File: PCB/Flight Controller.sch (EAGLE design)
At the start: 10 parts, among them J1 ZX62-AB-5PA(31), J2 M50-3600542R, U1 BMP390L, U2 NINA-B306, U3 LMS8117ADT-3.3, U4 BNO055

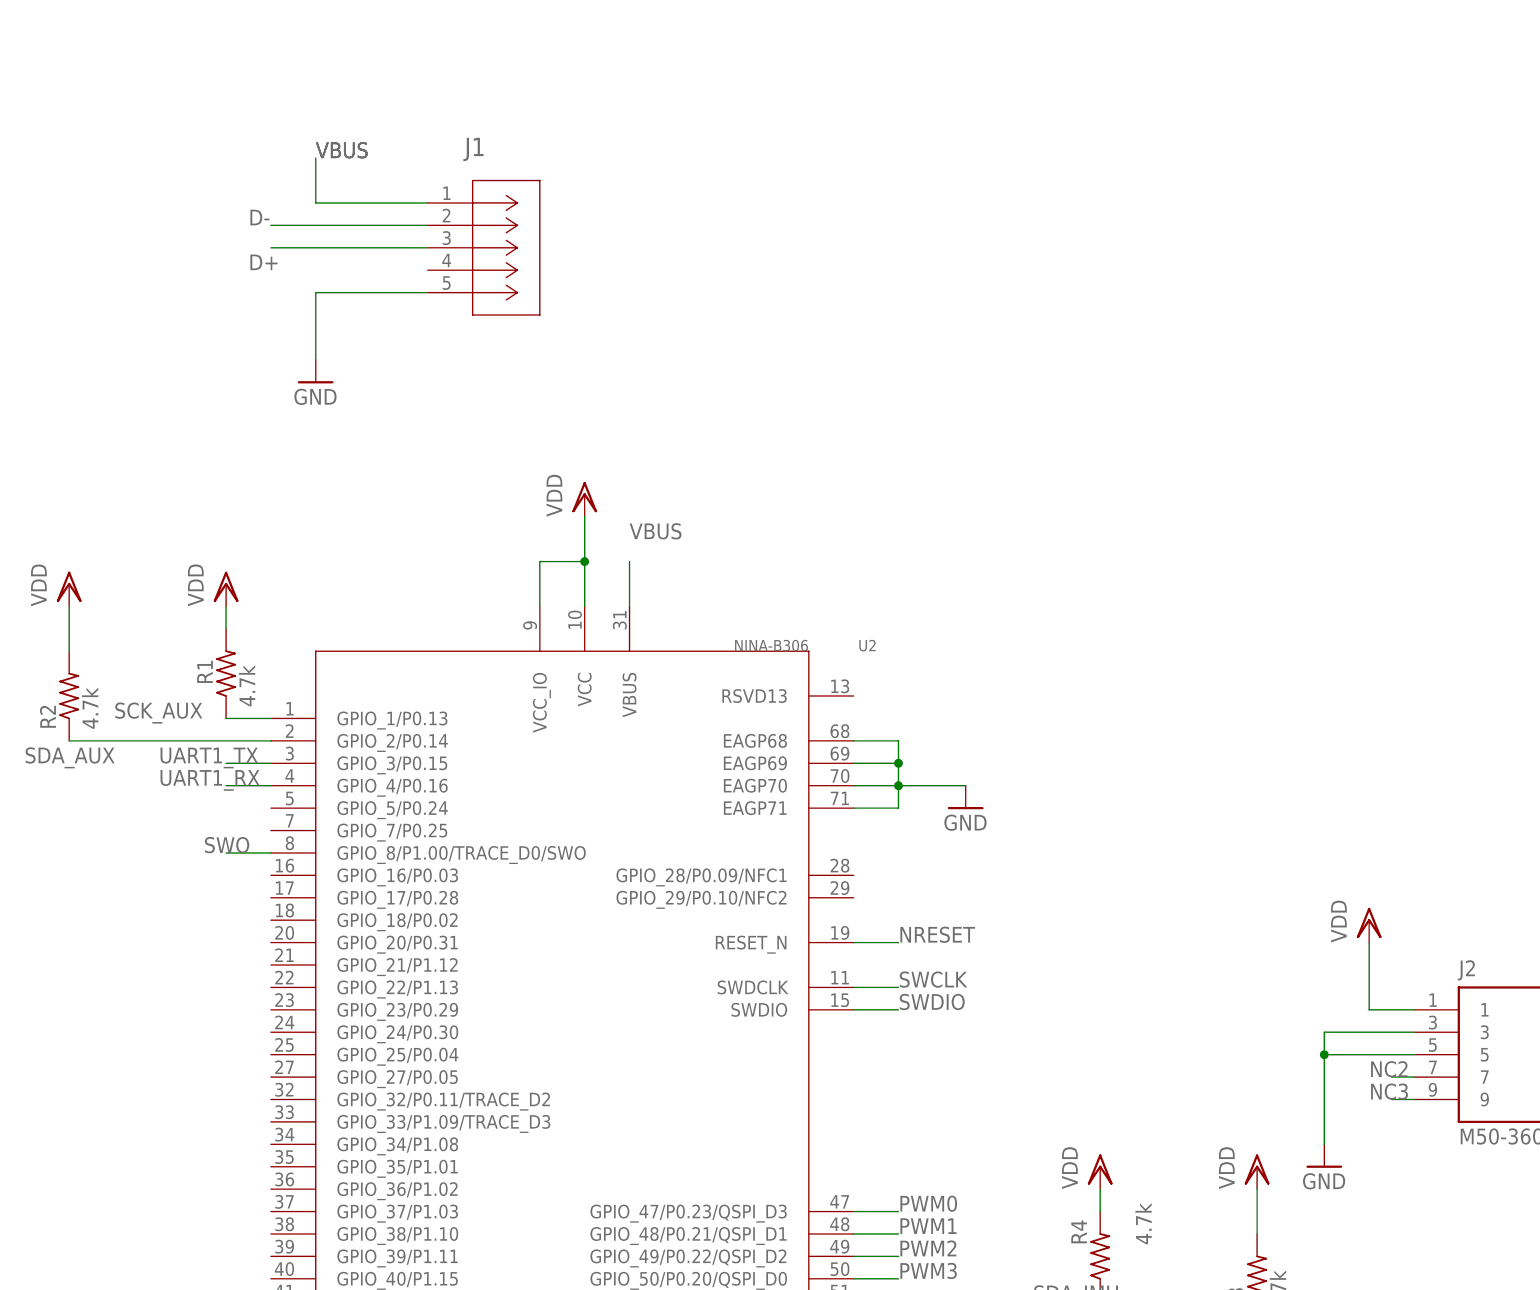
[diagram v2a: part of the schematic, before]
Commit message: added LEDs to PCB
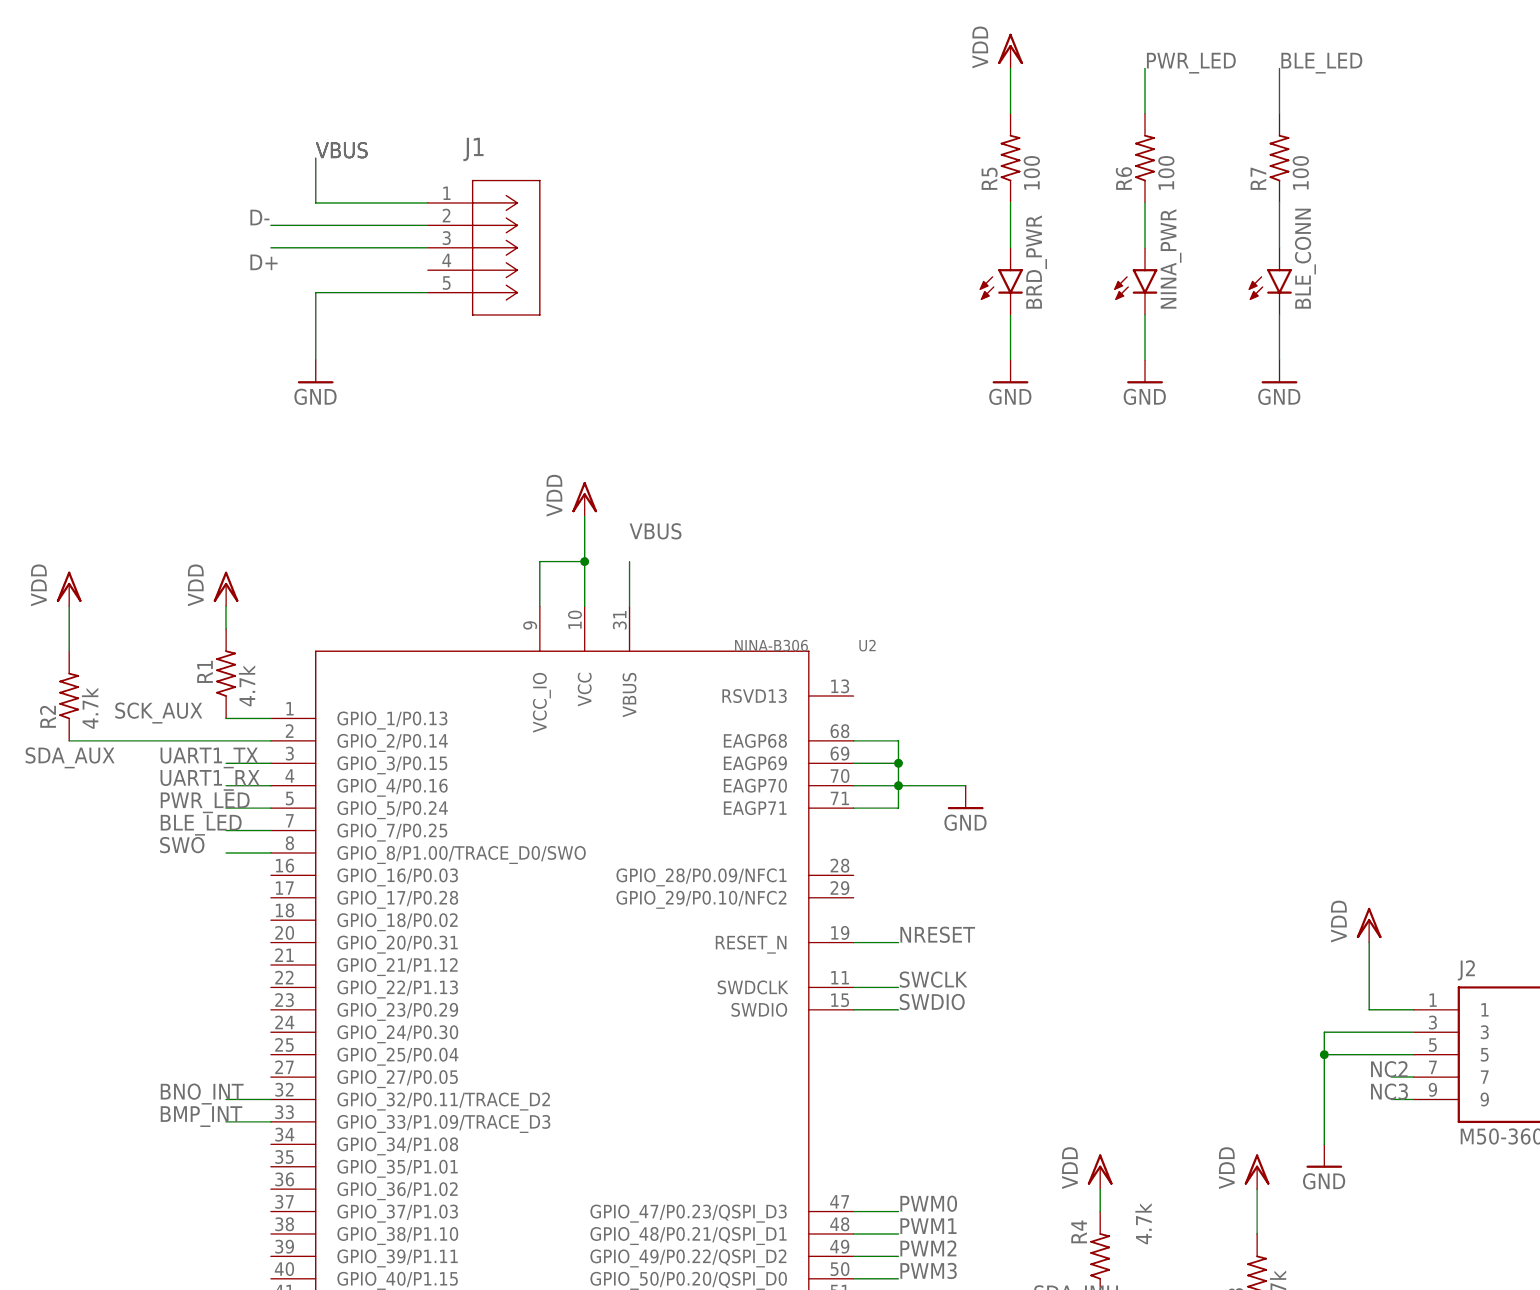
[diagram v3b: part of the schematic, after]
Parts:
- added BLE_CONN, BRD_PWR, NINA_PWR: (no value), led:LEDCHIPLED_1206
- added R5, R6, R7: 100, rcl:R-US_R1206
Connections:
- new net BLE_LED: R7.2, U2.GPIO_7/P0.25
- new net N$1: BRD_PWR.A, R5.1
- new net N$2: NINA_PWR.A, R6.1
- new net N$3: BLE_CONN.A, R7.1
- new net PWR_LED: R6.2, U2.GPIO_5/P0.24
- net BMP_INT: now also U2.GPIO_33/P1.09/TRACE_D3
- net BNO_INT: now also U2.GPIO_32/P0.11/TRACE_D2
- net GND: now also BLE_CONN.C, BRD_PWR.C, NINA_PWR.C
- net VDD: now also R5.2
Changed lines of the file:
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@@
 <part name="VDD10" library="supply1" library_urn="urn:adsk.eagle:library:371" deviceset="VDD" device=""/>
 <part name="VDD11" library="supply1" library_urn="urn:adsk.eagle:library:371" deviceset="VDD" device=""/>
+<part name="BRD_PWR" library="led" library_urn="urn:adsk.eagle:library:259" deviceset="LED" device="CHIPLED_1206" package3d_urn="urn:adsk.eagle:package:15823/2"/>
+<part name="NINA_PWR" library="led" library_urn="urn:adsk.eagle:library:259" deviceset="LED" device="CHIPLED_1206" package3d_urn="urn:adsk.eagle:package:15823/2"/>
+<part name="BLE_CONN" library="led" library_urn="urn:adsk.eagle:library:259" deviceset="LED" device="CHIPLED_1206" package3d_urn="urn:adsk.eagle:package:15823/2"/>
+<part name="R5" library="rcl" library_urn="urn:adsk.eagle:library:334" deviceset="R-US_" device="R1206" package3d_urn="urn:adsk.eagle:package:23540/2" value="100"/>
+<part name="R6" library="rcl" library_urn="urn:adsk.eagle:library:334" deviceset="R-US_" device="R1206" package3d_urn="urn:adsk.eagle:package:23540/2" value="100"/>
+<part name="R7" library="rcl" library_urn="urn:adsk.eagle:library:334" deviceset="R-US_" device="R1206" package3d_urn="urn:adsk.eagle:package:23540/2" value="100"/>
+<part name="GND10" library="supply1" library_urn="urn:adsk.eagle:library:371" deviceset="GND" device=""/>
+<part name="GND11" library="supply1" library_urn="urn:adsk.eagle:library:371" deviceset="GND" device=""/>
+<part name="GND12" library="supply1" library_urn="urn:adsk.eagle:library:371" deviceset="GND" device=""/>
+<part name="VDD12" library="supply1" library_urn="urn:adsk.eagle:library:371" deviceset="VDD" device=""/>
 </parts>
 <sheets>
@@
 <attribute name="VALUE" x="284.48" y="58.42" size="1.778" layer="96" rot="R90"/>
 </instance>
+<instance part="BRD_PWR" gate="G$1" x="259.08" y="162.56" smashed="yes">
+<attribute name="NAME" x="262.636" y="157.988" size="1.778" layer="95" rot="R90"/>
+<attribute name="VALUE" x="264.795" y="157.988" size="1.778" layer="96" rot="R90"/>
+</instance>
+<instance part="NINA_PWR" gate="G$1" x="274.32" y="162.56" smashed="yes">
+<attribute name="NAME" x="277.876" y="157.988" size="1.778" layer="95" rot="R90"/>
+<attribute name="VALUE" x="280.035" y="157.988" size="1.778" layer="96" rot="R90"/>
+</instance>
+<instance part="BLE_CONN" gate="G$1" x="289.56" y="162.56" smashed="yes">
+<attribute name="NAME" x="293.116" y="157.988" size="1.778" layer="95" rot="R90"/>
+<attribute name="VALUE" x="295.275" y="157.988" size="1.778" layer="96" rot="R90"/>
+</instance>
+<instance part="R5" gate="G$1" x="259.08" y="175.26" smashed="yes" rot="R90">
+<attribute name="NAME" x="257.5814" y="171.45" size="1.778" layer="95" rot="R90"/>
+<attribute name="VALUE" x="262.382" y="171.45" size="1.778" layer="96" rot="R90"/>
+</instance>
+<instance part="R6" gate="G$1" x="274.32" y="175.26" smashed="yes" rot="R90">
+<attribute name="NAME" x="272.8214" y="171.45" size="1.778" layer="95" rot="R90"/>
+<attribute name="VALUE" x="277.622" y="171.45" size="1.778" layer="96" rot="R90"/>
+</instance>
+<instance part="R7" gate="G$1" x="289.56" y="175.26" smashed="yes" rot="R90">
+<attribute name="NAME" x="288.0614" y="171.45" size="1.778" layer="95" rot="R90"/>
+<attribute name="VALUE" x="292.862" y="171.45" size="1.778" layer="96" rot="R90"/>
+</instance>
+<instance part="GND10" gate="1" x="259.08" y="149.86" smashed="yes">
+<attribute name="VALUE" x="256.54" y="147.32" size="1.778" layer="96"/>
+</instance>
+<instance part="GND11" gate="1" x="274.32" y="149.86" smashed="yes">
+<attribute name="VALUE" x="271.78" y="147.32" size="1.778" layer="96"/>
+</instance>
+<instance part="GND12" gate="1" x="289.56" y="149.86" smashed="yes">
+<attribute name="VALUE" x="287.02" y="147.32" size="1.778" layer="96"/>
+</instance>
+<instance part="VDD12" gate="G$1" x="259.08" y="187.96" smashed="yes">
+<attribute name="VALUE" x="256.54" y="185.42" size="1.778" layer="96" rot="R90"/>
+</instance>
 </instances>
 <busses>
@@
 <wire x1="287.02" y1="53.34" x2="287.02" y2="58.42" width="0.1524" layer="91"/>
 <pinref part="VDD11" gate="G$1" pin="VDD"/>
+</segment>
+<segment>
+<pinref part="R5" gate="G$1" pin="2"/>
+<pinref part="VDD12" gate="G$1" pin="VDD"/>
+<wire x1="259.08" y1="185.42" x2="259.08" y2="180.34" width="0.1524" layer="91"/>
 </segment>
 </net>
@@
 <junction x="71.12" y="55.88"/>
 </segment>
+<segment>
+<pinref part="BRD_PWR" gate="G$1" pin="C"/>
+<wire x1="259.08" y1="157.48" x2="259.08" y2="152.4" width="0.1524" layer="91"/>
+<pinref part="GND10" gate="1" pin="GND"/>
+</segment>
+<segment>
+<pinref part="NINA_PWR" gate="G$1" pin="C"/>
+<wire x1="274.32" y1="157.48" x2="274.32" y2="152.4" width="0.1524" layer="91"/>
+<pinref part="GND11" gate="1" pin="GND"/>
+</segment>
+<segment>
+<pinref part="BLE_CONN" gate="G$1" pin="C"/>
+<wire x1="289.56" y1="157.48" x2="289.56" y2="152.4" width="0.1524" layer="91"/>
+<pinref part="GND12" gate="1" pin="GND"/>
+</segment>
 </net>
 <net name="D-" class="0">
@@
 <pinref part="U2" gate="A" pin="GPIO_8/P1.00/TRACE_D0/SWO"/>
 <wire x1="175.26" y1="96.52" x2="170.18" y2="96.52" width="0.1524" layer="91"/>
-<label x="167.64" y="96.52" size="1.778" layer="95"/>
+<label x="162.56" y="96.52" size="1.778" layer="95"/>
 </segment>
 </net>
@@
 <wire x1="121.92" y1="68.58" x2="127" y2="68.58" width="0.1524" layer="91"/>
 <label x="127" y="68.58" size="1.778" layer="95"/>
+</segment>
+<segment>
+<pinref part="U2" gate="A" pin="GPIO_32/P0.11/TRACE_D2"/>
+<wire x1="175.26" y1="68.58" x2="170.18" y2="68.58" width="0.1524" layer="91"/>
+<label x="162.56" y="68.58" size="1.778" layer="95"/>
 </segment>
 </net>
@@
 <label x="129.54" y="147.32" size="1.778" layer="95"/>
 </segment>
+<segment>
+<pinref part="U2" gate="A" pin="GPIO_33/P1.09/TRACE_D3"/>
+<wire x1="175.26" y1="66.04" x2="170.18" y2="66.04" width="0.1524" layer="91"/>
+<label x="162.56" y="66.04" size="1.778" layer="95"/>
+</segment>
 </net>
 <net name="NC3" class="0">
@@
 </segment>
 </net>
+<net name="N$1" class="0">
+<segment>
+<pinref part="R5" gate="G$1" pin="1"/>
+<pinref part="BRD_PWR" gate="G$1" pin="A"/>
+<wire x1="259.08" y1="170.18" x2="259.08" y2="165.1" width="0.1524" layer="91"/>
+</segment>
+</net>
+<net name="N$2" class="0">
+<segment>
+<pinref part="R6" gate="G$1" pin="1"/>
+<pinref part="NINA_PWR" gate="G$1" pin="A"/>
+<wire x1="274.32" y1="170.18" x2="274.32" y2="165.1" width="0.1524" layer="91"/>
+</segment>
+</net>
+<net name="N$3" class="0">
+<segment>
+<pinref part="R7" gate="G$1" pin="1"/>
+<pinref part="BLE_CONN" gate="G$1" pin="A"/>
+<wire x1="289.56" y1="170.18" x2="289.56" y2="165.1" width="0.1524" layer="91"/>
+</segment>
+</net>
+<net name="PWR_LED" class="0">
+<segment>
+<pinref part="R6" gate="G$1" pin="2"/>
+<wire x1="274.32" y1="180.34" x2="274.32" y2="185.42" width="0.1524" layer="91"/>
+<label x="274.32" y="185.42" size="1.778" layer="95"/>
+</segment>
+<segment>
+<pinref part="U2" gate="A" pin="GPIO_5/P0.24"/>
+<wire x1="175.26" y1="101.6" x2="170.18" y2="101.6" width="0.1524" layer="91"/>
+<label x="162.56" y="101.6" size="1.778" layer="95"/>
+</segment>
+</net>
+<net name="BLE_LED" class="0">
+<segment>
+<pinref part="R7" gate="G$1" pin="2"/>
+<wire x1="289.56" y1="180.34" x2="289.56" y2="185.42" width="0.1524" layer="91"/>
+<label x="289.56" y="185.42" size="1.778" layer="95"/>
+</segment>
+<segment>
+<pinref part="U2" gate="A" pin="GPIO_7/P0.25"/>
+<wire x1="175.26" y1="99.06" x2="170.18" y2="99.06" width="0.1524" layer="91"/>
+<label x="162.56" y="99.06" size="1.778" layer="95"/>
+</segment>
+</net>

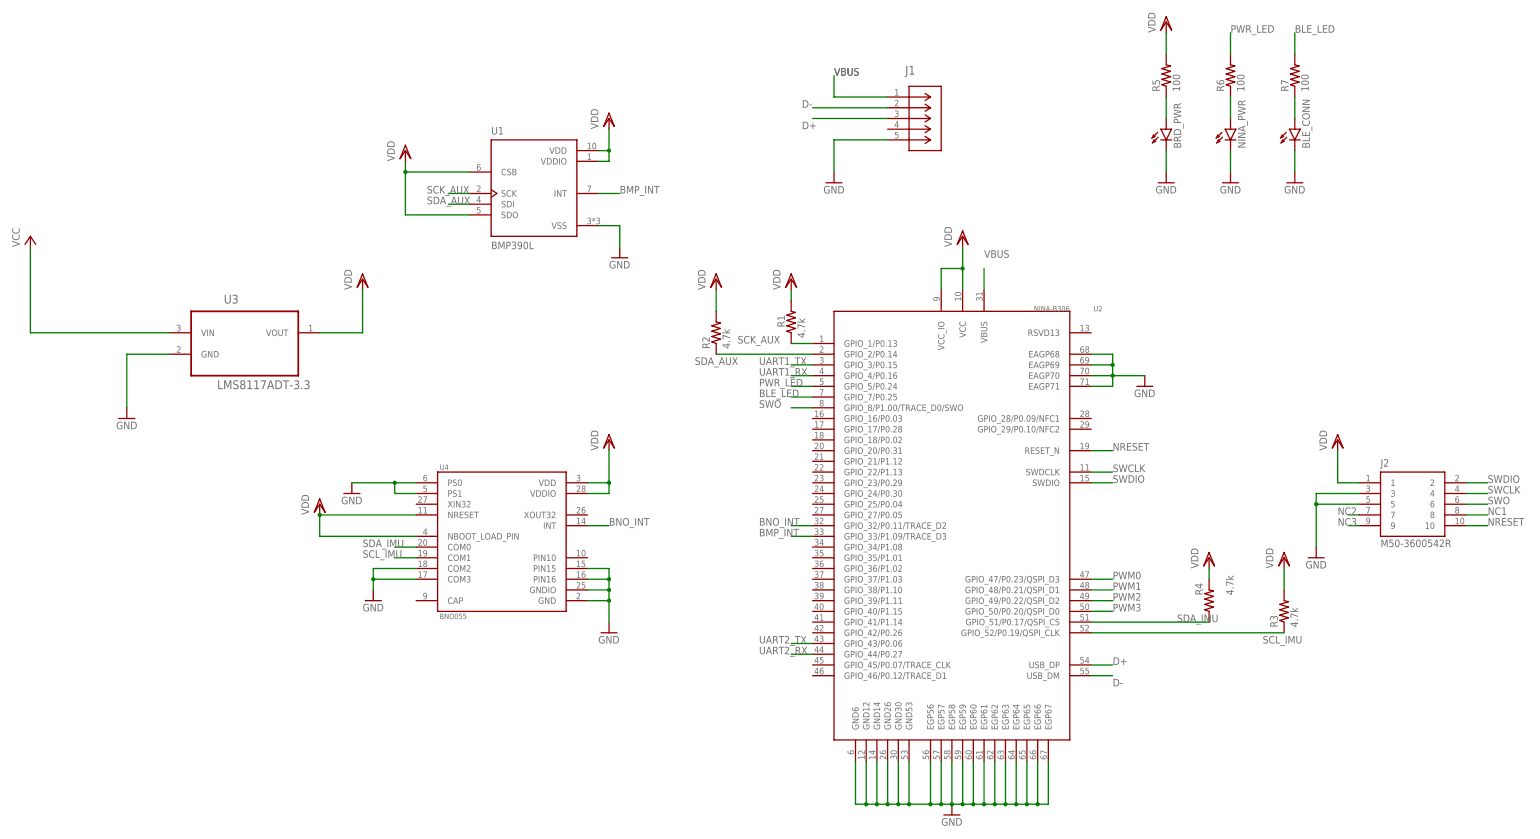
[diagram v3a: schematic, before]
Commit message: Added required capacitors to begin board layout
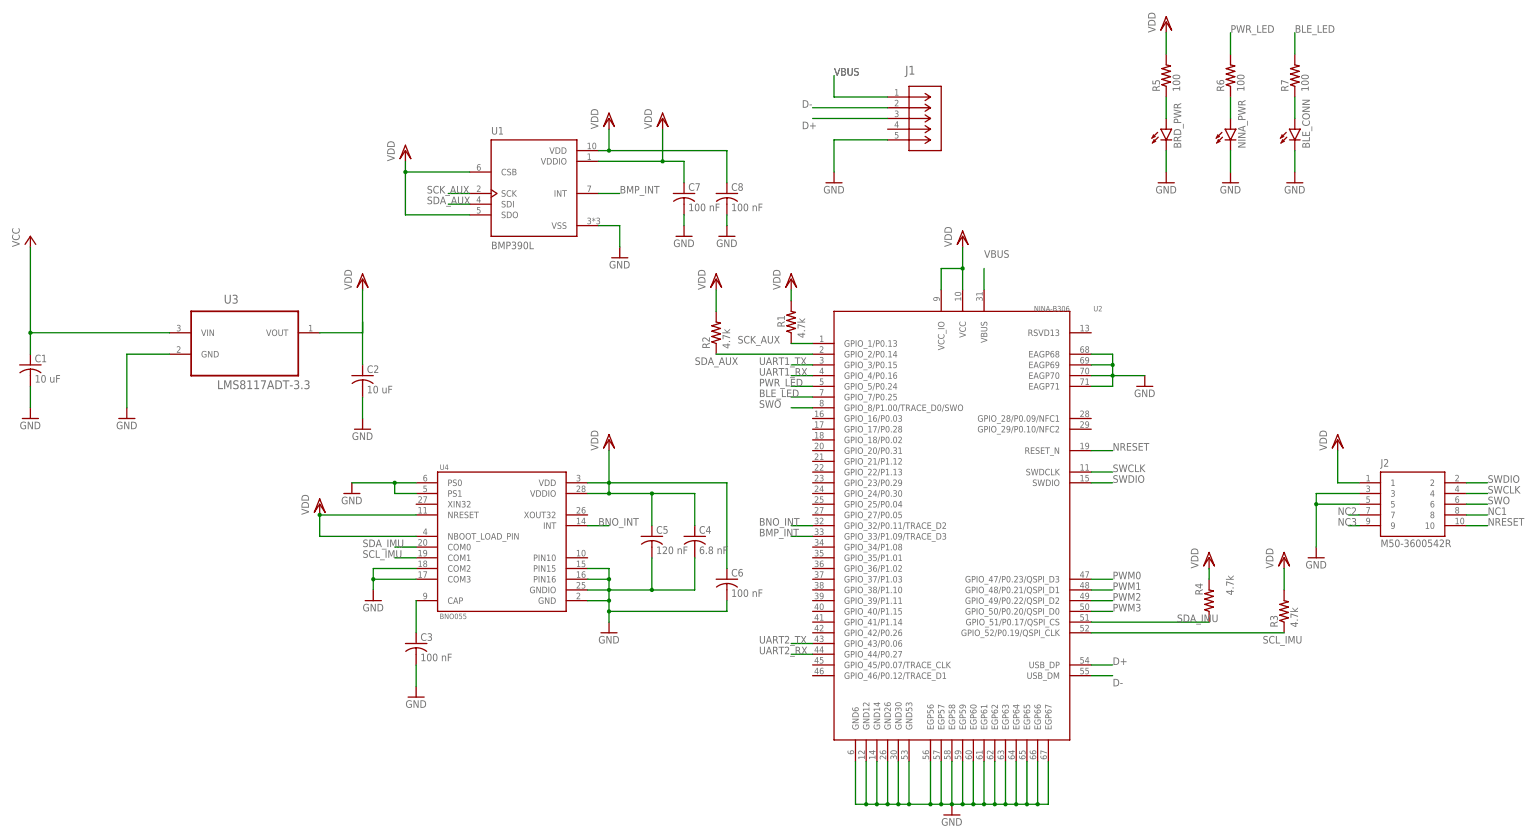
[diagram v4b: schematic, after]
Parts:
- added C1, C2: 10 uF, rcl:C-USC1206
- added C3, C6, C7, C8: 100 nF, rcl:C-USC1206
- added C4: 6.8 nF, rcl:C-USC1206
- added C5: 120 nF, rcl:C-USC1206
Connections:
- new net N$4: C3.1, U4.CAP
- new net VCC1: C2.1
- net GND: now also C1.2, C2.2, C3.2, C4.2, C5.2, C6.2, C7.2, C8.2
- net VCC: now also C1.1
- net VDD: now also C4.1, C5.1, C6.1, C7.1, C8.1
